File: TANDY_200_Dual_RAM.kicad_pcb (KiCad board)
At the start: 2 copper layers, 35.6 x 25.7 mm, 5 parts, among them J1 Conn_01x01_Male, J2 TANDY_26-3688, U1 628128_SOP32, U2 74LVC1G08

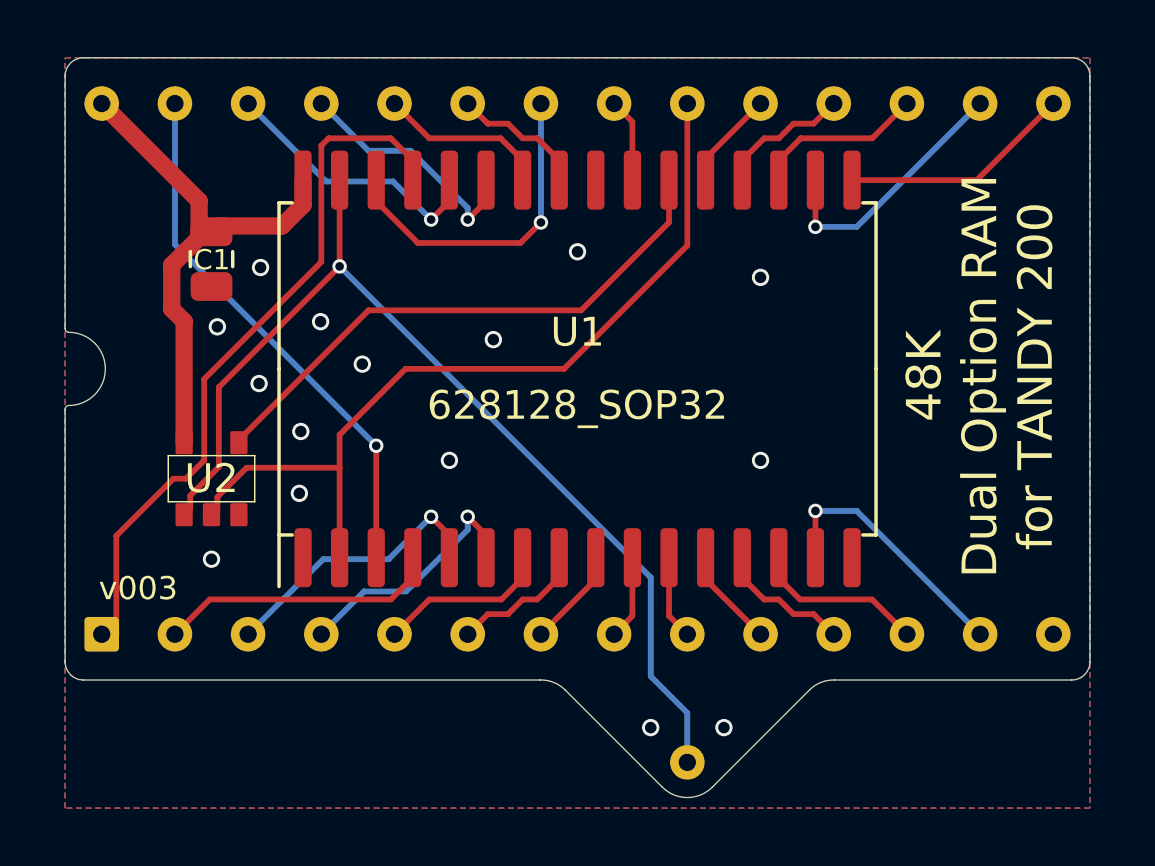
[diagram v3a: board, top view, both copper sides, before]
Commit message: 24k tsop layout and all board outlines expanded slightly
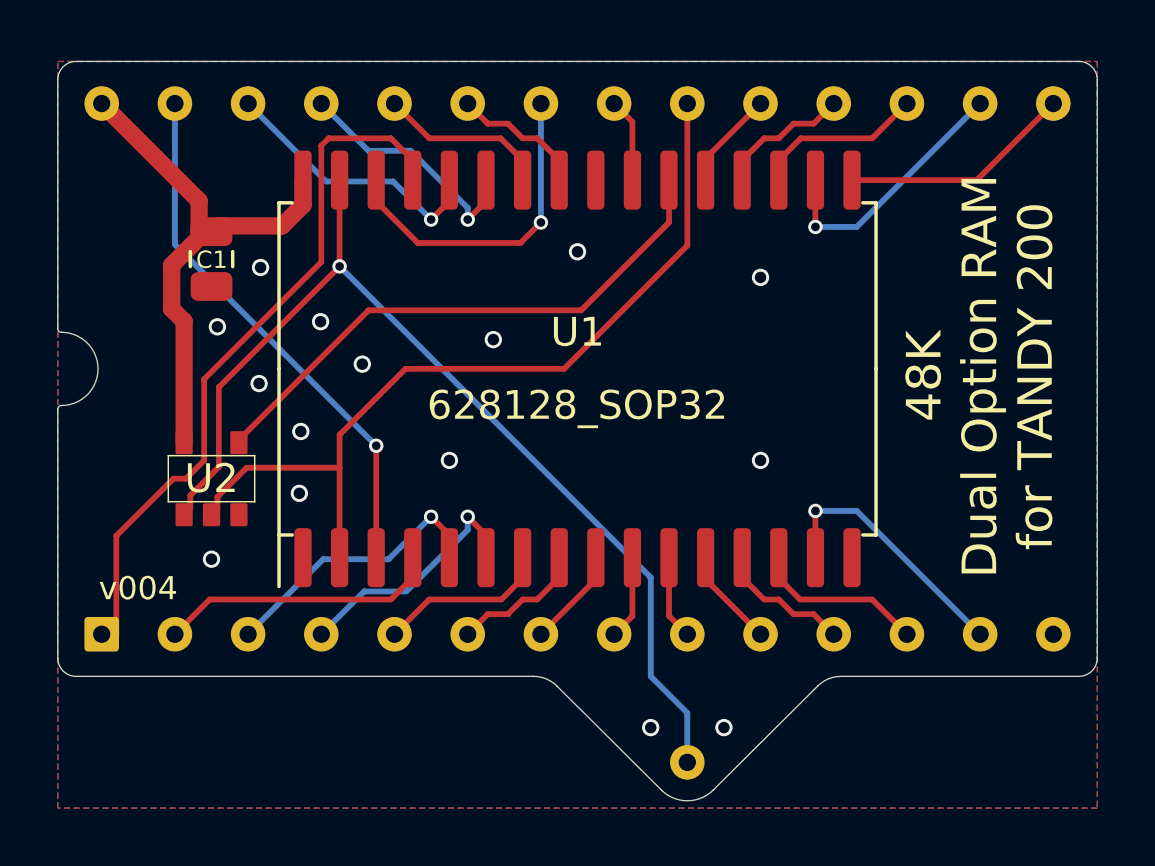
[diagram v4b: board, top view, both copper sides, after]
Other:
- board size 35.6 x 25.7 mm -> 36.1 x 25.7 mm
- board text added: "C1: ${91f0851b-88d9-4f00-a08c-ede0bdd24da4:VALUE} U2: ${eda52ffc-b211-43e3-a91c-151a6f13f97e:VALUE} PINS: Mill-Max 3121 or TE 1544210"
- board text removed: "C1: 0.1uF U2: 74LVC1G08 SOT-23-5 PINS: Mill-Max 3121 or TE 1544210"
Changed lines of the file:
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@@
   (title_block
     (title "TANDY 200 Dual RAM")
-    (date "2022-09-21")
-    (rev "003")
+    (date "2022-10-01")
+    (rev "004")
     (company "b.kenyon.w@gmail.com")
     (comment 1 "github.com/bkw777/TANDY_200_RAM")
@@
     (attr smd)
     (fp_text reference "C1" (at 0.028 -0.009) (layer "F.SilkS")
-      (effects (font (size 0.7 0.7) (thickness 0.1)))
+      (effects (font (size 0.6 0.6) (thickness 0.08)))
     )
     (fp_text value "0.1uF" (at 0 1.68 90) (layer "F.Fab") hide
@@
     )
   )
-  (gr_line (start 151.993599 113.576099) (end 155.3718 110.197901) (layer "Edge.Cuts") (width 0.01))
-  (gr_arc (start 155.3718 110.197901) (mid 155.768182 109.937249) (end 156.2354 109.855) (layer "Edge.Cuts") (width 0.01))
-  (gr_arc (start 151.993599 113.576099) (mid 151.13 113.933813) (end 150.266401 113.576099) (layer "Edge.Cuts") (width 0.01))
-  (gr_line (start 146.8882 110.197901) (end 150.266401 113.576099) (layer "Edge.Cuts") (width 0.01))
-  (gr_arc (start 129.667 97.79) (mid 129.577197 97.752803) (end 129.54 97.663) (layer "Edge.Cuts") (width 0.01))
-  (gr_line (start 156.2354 109.855) (end 164.465 109.855) (layer "Edge.Cuts") (width 0.01))
-  (gr_line (start 164.465 88.265) (end 130.175 88.265) (layer "Edge.Cuts") (width 0.01))
-  (gr_line (start 129.54 100.457) (end 129.54 109.22) (layer "Edge.Cuts") (width 0.01))
-  (gr_line (start 146.0246 109.855) (end 130.175 109.855) (layer "Edge.Cuts") (width 0.01))
-  (gr_arc (start 129.54 100.457) (mid 129.577197 100.367197) (end 129.667 100.33) (layer "Edge.Cuts") (width 0.01))
-  (gr_arc (start 164.465 88.265) (mid 164.914013 88.450987) (end 165.1 88.9) (layer "Edge.Cuts") (width 0.01))
-  (gr_arc (start 129.54 88.9) (mid 129.725987 88.450987) (end 130.175 88.265) (layer "Edge.Cuts") (width 0.01))
-  (gr_arc (start 129.667 97.79) (mid 130.937 99.06) (end 129.667 100.33) (layer "Edge.Cuts") (width 0.01))
-  (gr_line (start 165.1 109.22) (end 165.1 88.9) (layer "Edge.Cuts") (width 0.01))
-  (gr_arc (start 146.0246 109.855) (mid 146.491818 109.937249) (end 146.8882 110.197901) (layer "Edge.Cuts") (width 0.01))
-  (gr_arc (start 130.175 109.855) (mid 129.725987 109.669013) (end 129.54 109.22) (layer "Edge.Cuts") (width 0.01))
-  (gr_arc (start 165.1 109.22) (mid 164.914013 109.669013) (end 164.465 109.855) (layer "Edge.Cuts") (width 0.01))
-  (gr_line (start 129.54 97.663) (end 129.54 88.9) (layer "Edge.Cuts") (width 0.01))
+  (gr_line (start 152.028026 113.674026) (end 155.655777 110.062777) (layer "Edge.Cuts") (width 0.01))
+  (gr_arc (start 129.413 97.79) (mid 129.323197 97.752803) (end 129.286 97.663) (layer "Edge.Cuts") (width 0.01))
+  (gr_line (start 156.464 109.728) (end 164.719 109.728) (layer "Edge.Cuts") (width 0.01))
+  (gr_line (start 164.719 88.392) (end 129.921 88.392) (layer "Edge.Cuts") (width 0.01))
+  (gr_line (start 129.286 100.457) (end 129.286 109.093) (layer "Edge.Cuts") (width 0.01))
+  (gr_arc (start 155.655777 110.062777) (mid 156.026593 109.815006) (end 156.464 109.728) (layer "Edge.Cuts") (width 0.01))
+  (gr_arc (start 152.028026 113.674026) (mid 151.13 114.046001) (end 150.231974 113.674026) (layer "Edge.Cuts") (width 0.01))
+  (gr_line (start 145.796 109.728) (end 129.921 109.728) (layer "Edge.Cuts") (width 0.01))
+  (gr_arc (start 129.286 100.457) (mid 129.323197 100.367197) (end 129.413 100.33) (layer "Edge.Cuts") (width 0.01))
+  (gr_arc (start 164.719 88.392) (mid 165.168013 88.577987) (end 165.354 89.027) (layer "Edge.Cuts") (width 0.01))
+  (gr_arc (start 129.286 89.027) (mid 129.471987 88.577987) (end 129.921 88.392) (layer "Edge.Cuts") (width 0.01))
+  (gr_arc (start 129.413 97.79) (mid 130.683 99.06) (end 129.413 100.33) (layer "Edge.Cuts") (width 0.01))
+  (gr_line (start 165.354 109.093) (end 165.354 89.027) (layer "Edge.Cuts") (width 0.01))
+  (gr_arc (start 129.921 109.728) (mid 129.471987 109.542013) (end 129.286 109.093) (layer "Edge.Cuts") (width 0.01))
+  (gr_arc (start 165.354 109.093) (mid 165.168013 109.542013) (end 164.719 109.728) (layer "Edge.Cuts") (width 0.01))
+  (gr_arc (start 145.796 109.728) (mid 146.233407 109.815006) (end 146.604223 110.062777) (layer "Edge.Cuts") (width 0.01))
+  (gr_line (start 129.286 97.663) (end 129.286 89.027) (layer "Edge.Cuts") (width 0.01))
+  (gr_line (start 150.231974 113.674026) (end 146.604223 110.062777) (layer "Edge.Cuts") (width 0.01))
   (gr_text "${COMMENT1}" (at 147.32 99.06) (layer "B.SilkS")
     (effects (font (size 0.8 0.8) (thickness 0.1)) (justify mirror))
   )
-  (gr_text "C1: 0.1uF\nU2: 74LVC1G08 SOT-23-5\nPINS: Mill-Max 3121 or TE 1544210" (at 163.195 103.505) (layer "B.SilkS")
+  (gr_text "C1: ${91f0851b-88d9-4f00-a08c-ede0bdd24da4:VALUE}\nU2: ${eda52ffc-b211-43e3-a91c-151a6f13f97e:VALUE}\nPINS: Mill-Max 3121 or TE 1544210" (at 163.195 103.505) (layer "B.SilkS")
     (effects (font (size 1 1) (thickness 0.15)) (justify left mirror))
   )
@@
     (polygon
       (pts
-        (xy 165.1 114.3)
-        (xy 129.54 114.3)
-        (xy 129.54 88.265)
-        (xy 165.1 88.265)
+        (xy 165.354 114.3)
+        (xy 129.286 114.3)
+        (xy 129.286 88.392)
+        (xy 165.354 88.392)
       )
     )
@@
     (polygon
       (pts
-        (xy 165.1 114.3)
-        (xy 129.54 114.3)
-        (xy 129.54 88.265)
-        (xy 165.1 88.265)
+        (xy 165.354 114.3)
+        (xy 129.286 114.3)
+        (xy 129.286 88.392)
+        (xy 165.354 88.392)
       )
     )
